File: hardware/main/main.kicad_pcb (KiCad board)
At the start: 4 copper layers, 71.8 x 109.5 mm, 243 parts, among them J101 ST_LINK, J102 USART, J301 Overvoltage_protection, J302 Rad_sensor, J303 Mos_temp, J304 Diode_temp, J601 Supplies, J801 RJ45_Shielded, J802 RJ45_Shielded, Q401 BSC093N15NS5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

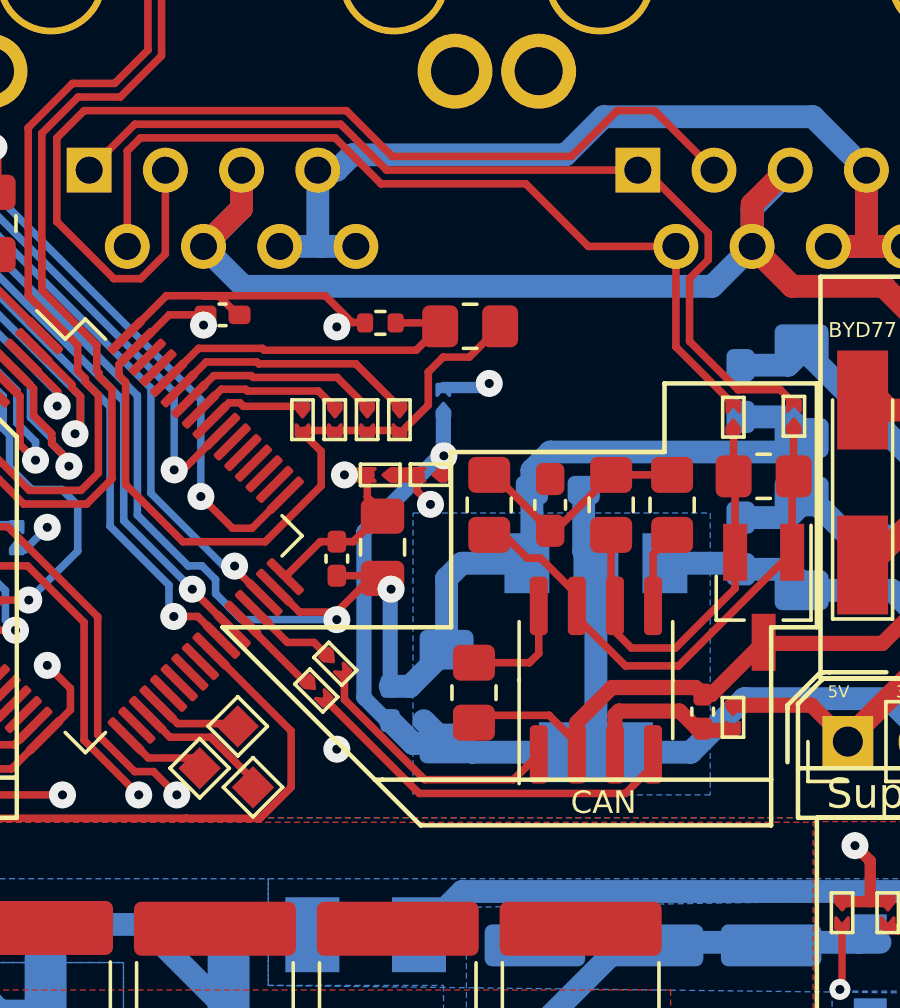
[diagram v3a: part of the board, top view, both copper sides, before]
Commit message: layout: fix path of heatsink (using relative path)
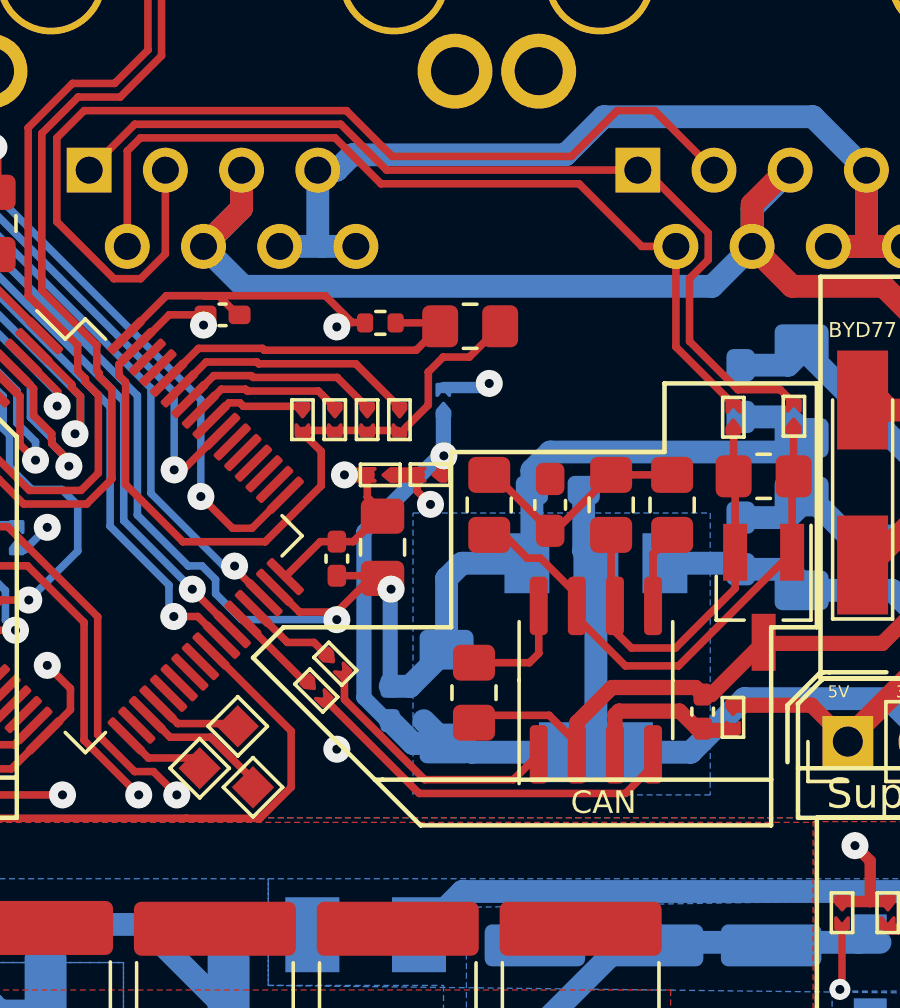
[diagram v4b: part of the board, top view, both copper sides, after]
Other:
- board text added: "Diode.°C"
